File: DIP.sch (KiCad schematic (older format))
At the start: 2 parts, among them SW21 SW_DIP_x08, U18 74LS244

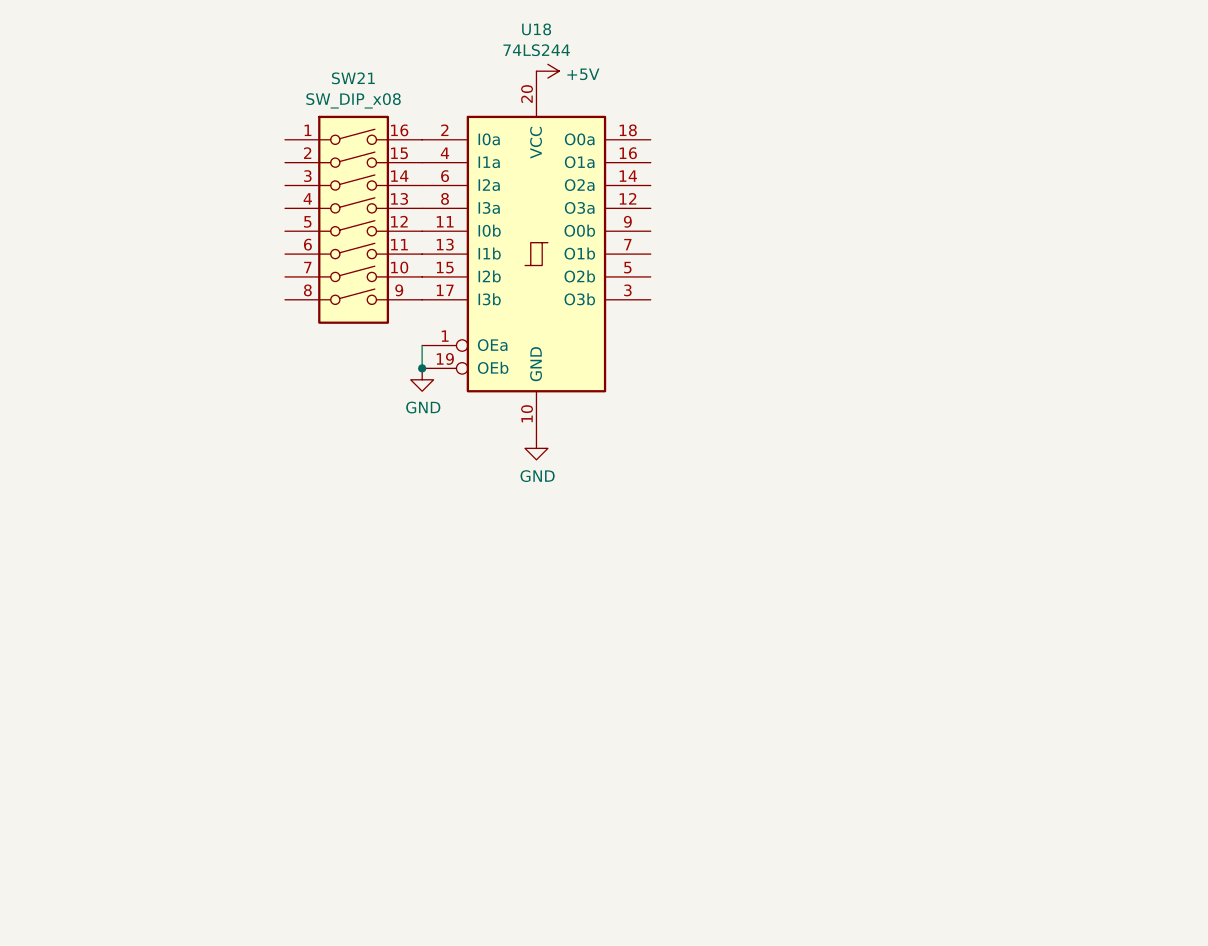
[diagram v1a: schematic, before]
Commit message: All schematics present
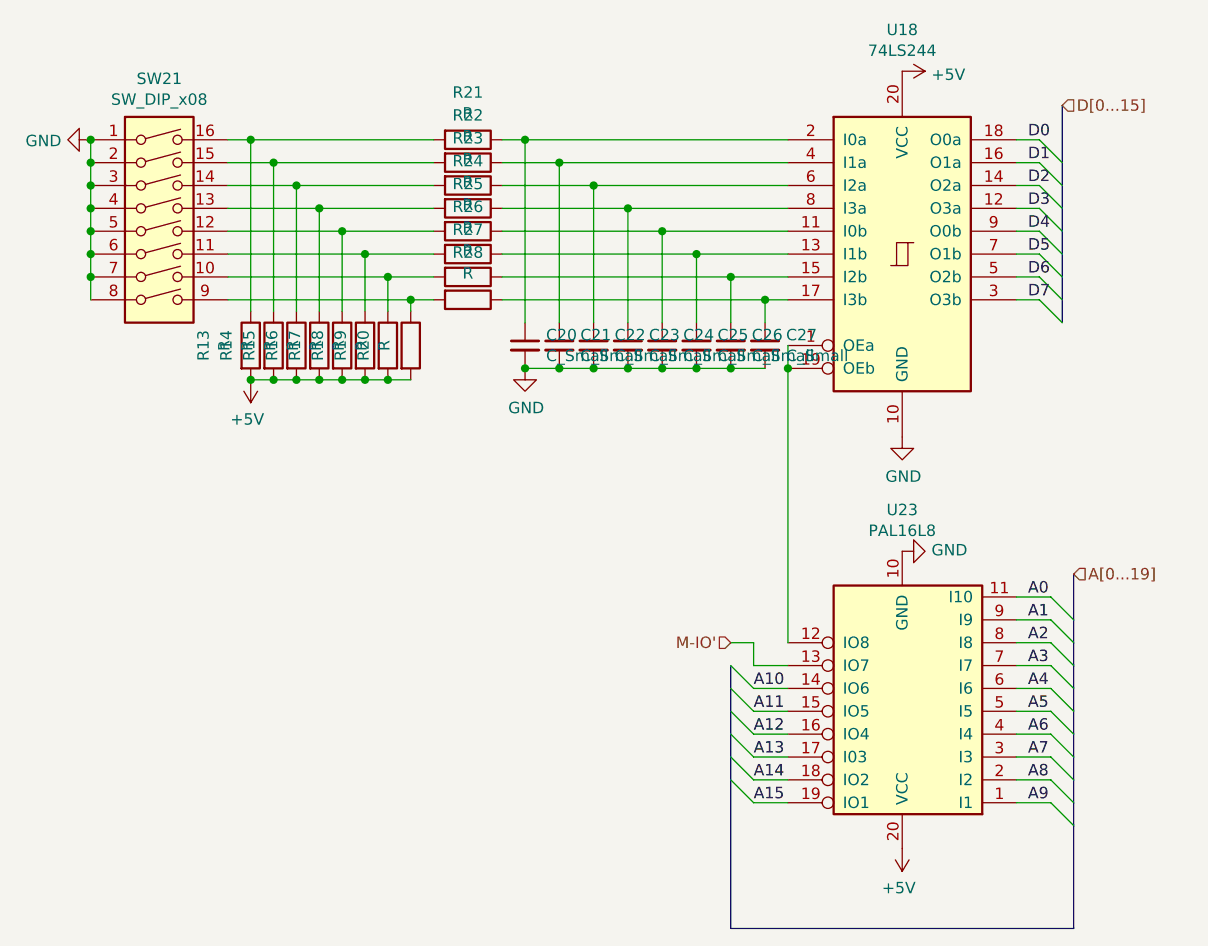
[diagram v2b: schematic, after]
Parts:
- added C20, C21, C22, C23, C24, C25, C26, C27: C_Small, symbol Device:C_Small
- added R13, R14, R15, R16, R17, R18, R19, R20, R21, R22, R23, R24, R25, R26, R27, R28: R, symbol Device:R
- added U23: PAL16L8, symbol Logic_Programmable:PAL16L8
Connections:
- net +5V: now also R13.2, R14.2, R15.2, R16.2, R17.2, R18.2, R19.2, R20.2, U23.20 (VCC)
- net GND: now also SW21.1, SW21.2, SW21.3, SW21.4, SW21.5, SW21.6, SW21.7, SW21.8, C20.2, C21.2, C22.2, C23.2, C24.2, C25.2, C26.2, C27.2, U23.10 (GND); no longer U18.1 (OEa), U18.19 (OEb)
- net at U18.11 (I0b): now also C24.1, R25.1; no longer SW21.12
- net D3: now reaches U18.12 (O3a)
- net at U18.13 (I1b): now also C25.1, R26.1; no longer SW21.11
- net D2: now reaches U18.14 (O2a)
- net at U18.15 (I2b): now also C26.1, R27.1; no longer SW21.10
- net D1: now reaches U18.16 (O1a)
- net at U18.17 (I3b): now also C27.1, R28.1; no longer SW21.9
- net D0: now reaches U18.18 (O0a)
- net at U18.2 (I0a): now also C20.1, R21.1; no longer SW21.16
- net D7: now reaches U18.3 (O3b)
- net at U18.4 (I1a): now also C21.1, R22.1; no longer SW21.15
- net D6: now reaches U18.5 (O2b)
- net at U18.6 (I2a): now also C22.1, R23.1; no longer SW21.14
- net D5: now reaches U18.7 (O1b)
- net at U18.8 (I3a): now also C23.1, R24.1; no longer SW21.13
- net D4: now reaches U18.9 (O0b)
- new net: U18.1 (OEa), U18.19 (OEb), U23.12 (IO8)
- new net: R13.1, R21.2, SW21.16
- new net: R14.1, R22.2, SW21.15
- new net: R15.1, R23.2, SW21.14
- new net: R16.1, R24.2, SW21.13
- new net: R17.1, R25.2, SW21.12
- new net: R18.1, R26.2, SW21.11
- new net: R19.1, R27.2, SW21.10
- new net: R20.1, R28.2, SW21.9
- new net A0: U23.11 (I10)
- new net A1: U23.9 (I9)
- new net A10: U23.14 (IO6)
- new net A11: U23.15 (IO5)
- new net A12: U23.16 (IO4)
- new net A13: U23.17 (I03)
- new net A14: U23.18 (IO2)
- new net A15: U23.19 (IO1)
- new net A2: U23.8 (I8)
- new net A3: U23.7 (I7)
- new net A4: U23.6 (I6)
- new net A5: U23.5 (I5)
- new net A6: U23.4 (I4)
- new net A7: U23.3 (I3)
- new net A8: U23.2 (I2)
- new net A9: U23.1 (I1)
- new net M-IO': U23.13 (IO7)
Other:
- moved on the sheet: SW21, U18

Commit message: Started PCB
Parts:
- C18: renamed from C20; footprint (none) -> Capacitor_SMD:CP_Elec_3x5.3
- C19: renamed from C21; footprint (none) -> Capacitor_SMD:CP_Elec_3x5.3
- C20: renamed from C22; footprint (none) -> Capacitor_SMD:CP_Elec_3x5.3
- C21: renamed from C23; footprint (none) -> Capacitor_SMD:CP_Elec_3x5.3
- C22: renamed from C24; footprint (none) -> Capacitor_SMD:CP_Elec_3x5.3
- C23: renamed from C25; footprint (none) -> Capacitor_SMD:CP_Elec_3x5.3
- C24: renamed from C26; footprint (none) -> Capacitor_SMD:CP_Elec_3x5.3
- C25: renamed from C27; footprint (none) -> Capacitor_SMD:CP_Elec_3x5.3
- R13, R14, R15, R16, R17, R18, R19, R20, R21, R22, R23, R24, R25, R26, R27, R28: footprint (none) -> Resistor_SMD:R_0201_0603Metric
- SW21: footprint (none) -> Button_Switch_SMD:SW_DIP_SPSTx01_Slide_6.7x4.1mm_W6.73mm_P2.54mm_LowProfile_JPin
- U18: footprint (none) -> Package_DIP:DIP-20_W7.62mm
- U19: renamed from U23; footprint (none) -> Package_DIP:DIP-20_W7.62mm
